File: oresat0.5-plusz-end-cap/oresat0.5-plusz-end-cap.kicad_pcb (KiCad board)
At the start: 2 copper layers, 105.6 x 105.6 mm, 43 parts, among them J2 U.FL-R-SMA, U1 LTC4305, U2 MMC5983MA, U3 MMC5983MA

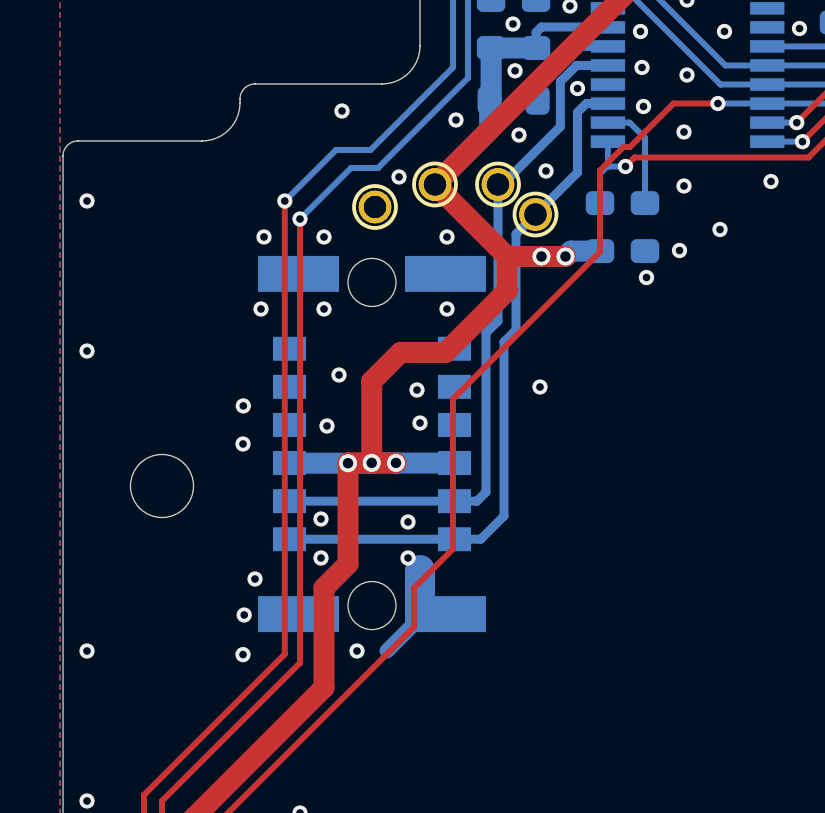
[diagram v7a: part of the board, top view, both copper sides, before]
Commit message: moved endcap harwin connectors on both +/-Z endcaps per move in Onshape
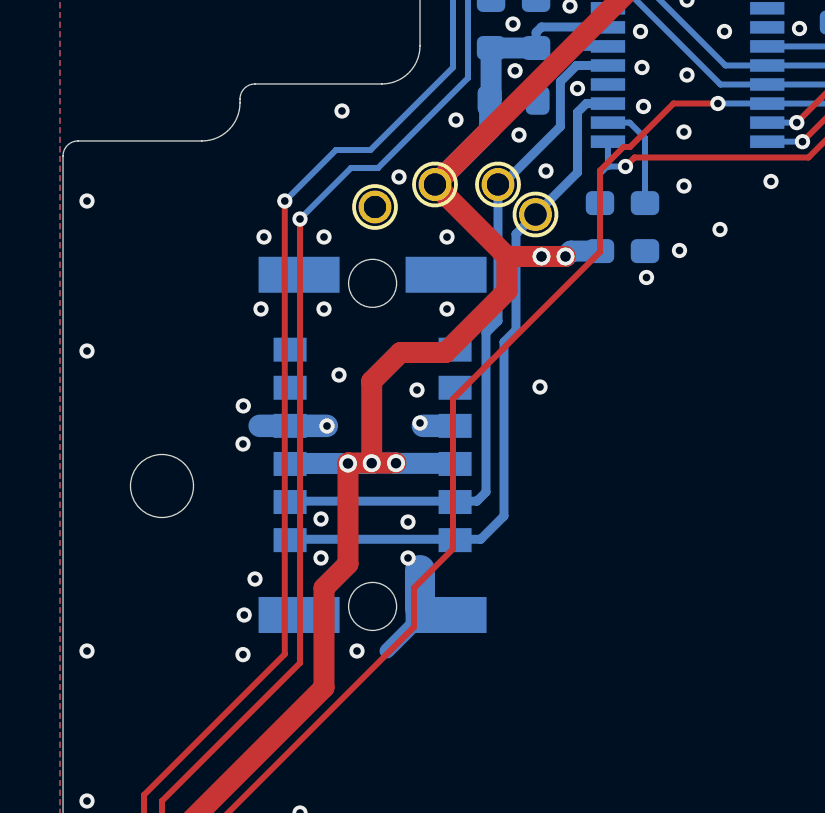
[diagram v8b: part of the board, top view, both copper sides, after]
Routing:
- net GND: track 3.42 -> 6.88 mm
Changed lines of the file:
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@@
 		(locked yes)
 		(layer "B.Cu")
-		(at 106 76.1 -90)
+		(at 106.02 76.13 -90)
 		(property "Reference" "J1"
 			(at 7.4 2.7 0)
@@
 	)
 	(gr_circle
-		(center 106 76.1)
-		(end 106.5 76.1)
+		(center 106.02 76.13)
+		(end 106.52 76.13)
 		(stroke
 			(width 0.002)
@@
 	)
 	(gr_line
-		(start 108.1 70.915)
-		(end 103.9 81.285)
+		(start 108.12 70.945)
+		(end 103.92 81.315)
 		(stroke
 			(width 0.002)
@@
 	)
 	(gr_line
-		(start 108.1 81.285)
-		(end 103.9 70.915)
+		(start 108.12 81.315)
+		(end 103.92 70.945)
 		(stroke
 			(width 0.002)
@@
 	)
 	(via
-		(at 105.2 76.74)
+		(at 105.2 76.75)
 		(size 0.604)
 		(drill 0.35)
@@
 	)
 	(via
-		(at 105.99 76.73)
+		(at 105.99 76.74)
 		(size 0.604)
 		(drill 0.35)
@@
 	)
 	(via
-		(at 106.8 76.73)
+		(at 106.8 76.74)
 		(size 0.604)
 		(drill 0.35)
@@
 	)
 	(segment
-		(start 105.98 76.74)
-		(end 103.255 76.74)
+		(start 105.98 76.75)
+		(end 103.255 76.75)
 		(width 0.7)
 		(layer "B.Cu")
@@
 	)
 	(segment
-		(start 106.8 76.73)
-		(end 105.99 76.73)
+		(start 106.8 76.74)
+		(end 105.99 76.74)
 		(width 0.7)
 		(layer "B.Cu")
@@
 	)
 	(segment
-		(start 108.75 76.735)
-		(end 106.805 76.735)
+		(start 108.75 76.745)
+		(end 106.805 76.745)
 		(width 0.7)
 		(layer "B.Cu")
@@
 	)
 	(segment
+		(start 108.77 75.495)
+		(end 107.695 75.495)
+		(width 0.75)
+		(layer "B.Cu")
+		(net 2)
+	)
+	(segment
+		(start 104.495 75.495)
+		(end 104.5 75.5)
+		(width 0.25)
+		(layer "B.Cu")
+		(net 2)
+	)
+	(segment
+		(start 102.255 75.495)
+		(end 102.25 75.5)
+		(width 0.5)
+		(layer "B.Cu")
+		(net 2)
+	)
+	(segment
+		(start 103.27 75.495)
+		(end 104.495 75.495)
+		(width 0.75)
+		(layer "B.Cu")
+		(net 2)
+	)
+	(segment
+		(start 103.27 75.495)
+		(end 102.255 75.495)
+		(width 0.75)
+		(layer "B.Cu")
+		(net 2)
+	)
+	(segment
 		(start 107.6 81.9)
 		(end 106.5 83)
@@
 	)
 	(segment
+		(start 107.695 75.495)
+		(end 107.6 75.4)
+		(width 0.25)
+		(layer "B.Cu")
+		(net 2)
+	)
+	(segment
 		(start 191.9 79.75)
 		(end 191.9 82.2)
@@
 	)
 	(segment
-		(start 108.75 78.005)
-		(end 103.25 78.005)
-		(width 0.3)
-		(layer "B.Cu")
-		(net 5)
-	)
-	(segment
-		(start 109.497668 78.005)
+		(start 109.8 72.4)
 		(end 109.8 77.702669)
 		(width 0.3)
@@
 	(segment
 		(start 109.8 77.702669)
-		(end 109.8 72.4)
-		(width 0.3)
-		(layer "B.Cu")
-		(net 5)
-	)
-	(segment
-		(start 110.2 72)
-		(end 110.2 67.45)
+		(end 109.497668 78.005)
 		(width 0.3)
 		(layer "B.Cu")
@@
 	)
 	(segment
-		(start 109.8 72.4)
-		(end 110.2 72)
+		(start 109.497668 78.005)
+		(end 103.25 78.005)
 		(width 0.3)
 		(layer "B.Cu")
@@
 	)
 	(segment
-		(start 108.75 78.005)
-		(end 109.497668 78.005)
+		(start 110.2 67.45)
+		(end 110.2 72)
 		(width 0.3)
 		(layer "B.Cu")
@@
 		(width 0.3)
 		(layer "B.Cu")
+		(net 5)
+	)
+	(segment
+		(start 110.2 72)
+		(end 109.8 72.4)
+		(width 0.3)
+		(layer "B.Cu")
